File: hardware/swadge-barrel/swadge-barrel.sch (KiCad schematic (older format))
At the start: 45 parts, among them J1 USB_B_Micro, SW1 SW_SPDT, U1 AP1117-33, U2 ESP-13-WROOM-02D, U3 BUS_PCIexpress, U4 OLED_CONNECTOR, U5 QMA6981, U6 OLED_DISPLAY

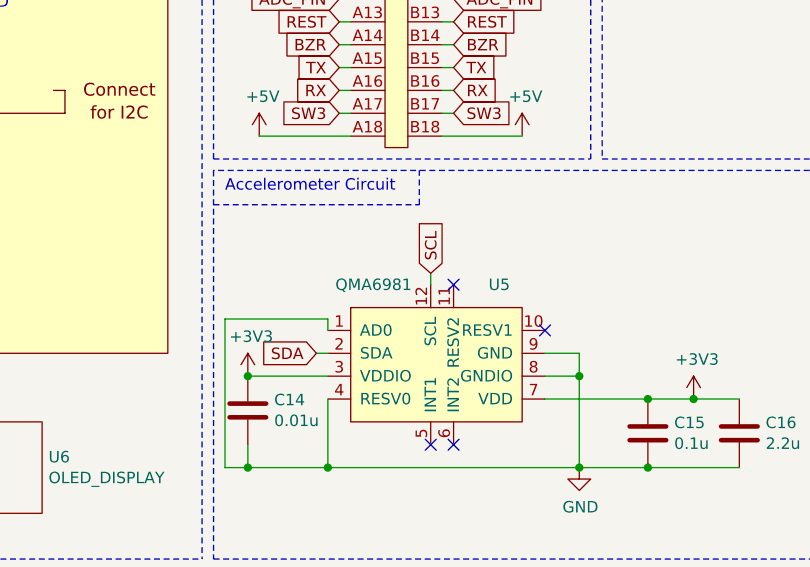
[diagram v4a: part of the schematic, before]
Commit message: Added series I2C resistors to QMA6981
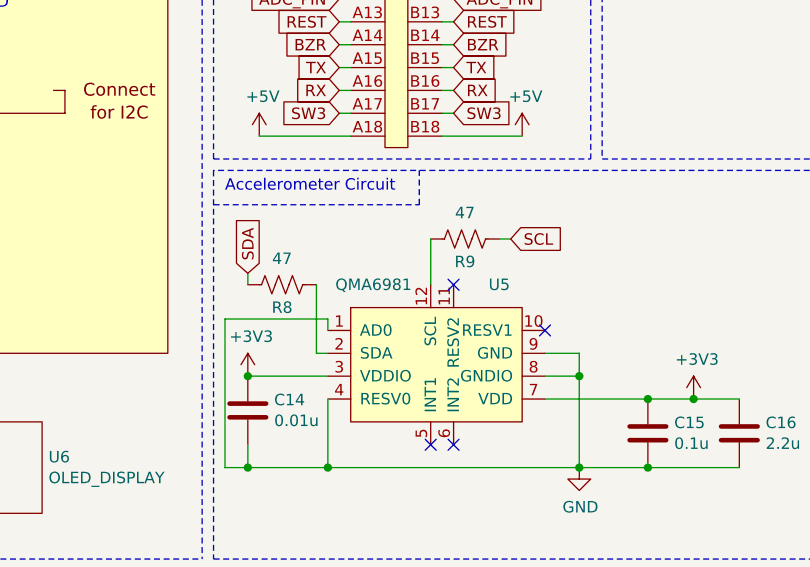
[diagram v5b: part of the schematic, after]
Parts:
- added R8, R9: 47, Swadge_Parts:R_0603_1608Metric, symbol Swadge_Parts:R_US
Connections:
- net SCL: now also R9.1; no longer U5.12 (SCL)
- net SDA: now also R8.2; no longer U5.2 (SDA)
- new net: R9.2, U5.12 (SCL)
- new net: R8.1, U5.2 (SDA)
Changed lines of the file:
@@
 	1    0    0    -1
 $EndComp
-Text GLabel 7350 5600 0    50   Input ~ 0
+Text GLabel 7050 5250 1    50   Input ~ 0
 SDA
-Text GLabel 7850 5250 1    50   Input ~ 0
+Text GLabel 8200 5100 2    50   Input ~ 0
 SCL
 NoConn ~ 7850 6000
@@
 	8800 6100 8500 6100
 Connection ~ 8800 6100
-Wire Wire Line
-	7850 5250 7850 5300
 Wire Wire Line
 	7350 5600 7400 5600
@@
 	1    0    0    -1
 $EndComp
+$Comp
+L Swadge_Parts:R_US R9
+U 1 1 5DCFA389
+P 8000 5100
+F 0 "R9" V 8100 5100 50  0000 C CNN
+F 1 "47" V 7886 5100 50  0000 C CNN
+F 2 "Swadge_Parts:R_0603_1608Metric" V 8040 5090 50  0001 C CNN
+F 3 "" H 8000 5100 50  0001 C CNN
+F 4 "10" H 6300 150 50  0001 C CNN "Cost100"
+F 5 "RMCF0603FT47R0TR-ND" H 6300 150 50  0001 C CNN "Digikey"
+F 6 "Y" H 6300 150 50  0001 C CNN "Substitutable"
+F 7 "0603 Package" H 8000 5100 50  0001 C CNN "Notes"
+	1    8000 5100
+	0    1    1    0
+$EndComp
+Wire Wire Line
+	8200 5100 8150 5100
+Wire Wire Line
+	7850 5100 7850 5300
+Wire Wire Line
+	7050 5250 7050 5300
+Wire Wire Line
+	7350 5300 7350 5600
+$Comp
+L Swadge_Parts:R_US R8
+U 1 1 5DD38085
+P 7200 5300
+F 0 "R8" V 7300 5300 50  0000 C CNN
+F 1 "47" V 7086 5300 50  0000 C CNN
+F 2 "Swadge_Parts:R_0603_1608Metric" V 7240 5290 50  0001 C CNN
+F 3 "" H 7200 5300 50  0001 C CNN
+F 4 "10" H 5500 350 50  0001 C CNN "Cost100"
+F 5 "RMCF0603FT47R0TR-ND" H 5500 350 50  0001 C CNN "Digikey"
+F 6 "Y" H 5500 350 50  0001 C CNN "Substitutable"
+F 7 "0603 Package" H 7200 5300 50  0001 C CNN "Notes"
+	1    7200 5300
+	0    1    1    0
+$EndComp
 $EndSCHEMATC

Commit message: Added new QMA6981 part with larger pads Updated banana and barrel with new pads
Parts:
- U5: footprint Swadge_Parts:QMA6981 -> Swadge_Parts:QMA6981_2
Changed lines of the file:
@@
 F 0 "U5" H 8150 6000 50  0000 C CNN
 F 1 "QMA6981" H 7600 6000 50  0000 C CNN
-F 2 "Swadge_Parts:QMA6981" H 7700 6350 50  0001 C CNN
+F 2 "Swadge_Parts:QMA6981_2" H 7700 6350 50  0001 C CNN
 F 3 "https://datasheet.lcsc.com/szlcsc/QST-QMA6981_C310611.pdf" H 7900 5600 50  0001 C CNN
 F 4 "LCSC Part #C310611" H 7600 6450 50  0001 C CNN "Digikey"
